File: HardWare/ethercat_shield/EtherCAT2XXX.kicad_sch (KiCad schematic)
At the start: 4 parts

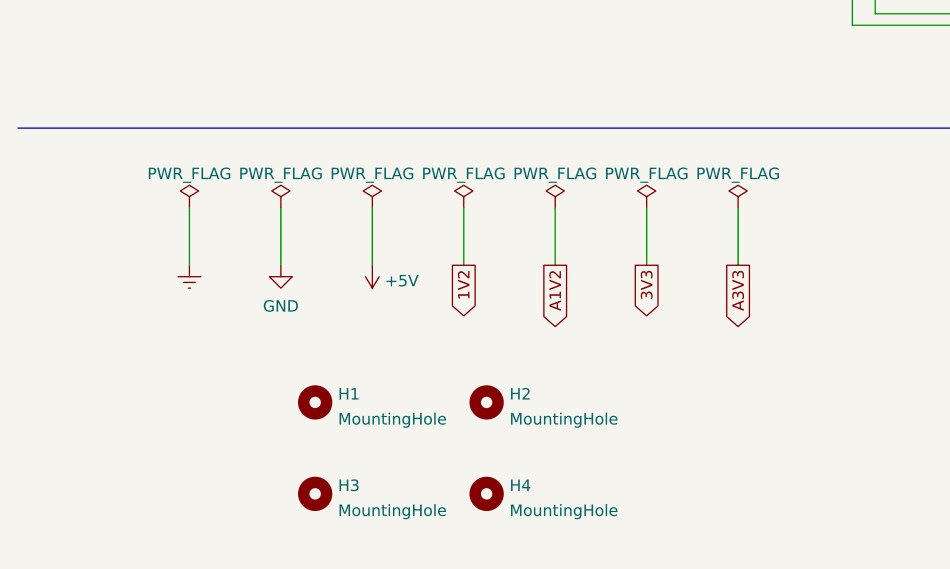
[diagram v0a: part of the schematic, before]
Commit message: 'ethercat_shield' PCB_layout completed
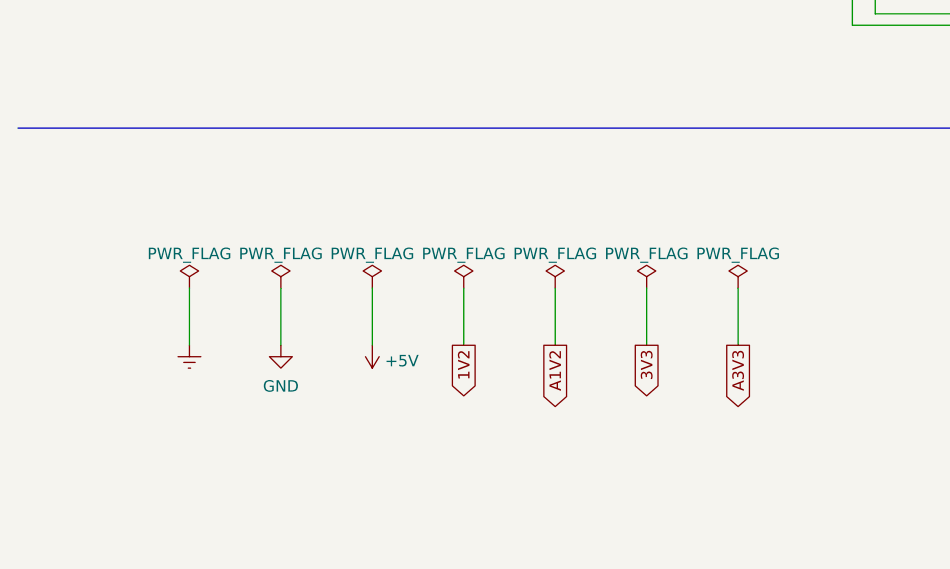
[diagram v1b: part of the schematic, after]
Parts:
- removed H1, H2, H3, H4: MountingHole, MountingHole:MountingHole_2.2mm_M2_DIN965_Pad, symbol Mechanical:MountingHole
